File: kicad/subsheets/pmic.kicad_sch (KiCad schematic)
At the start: 53 parts, among them U2 RK809-5

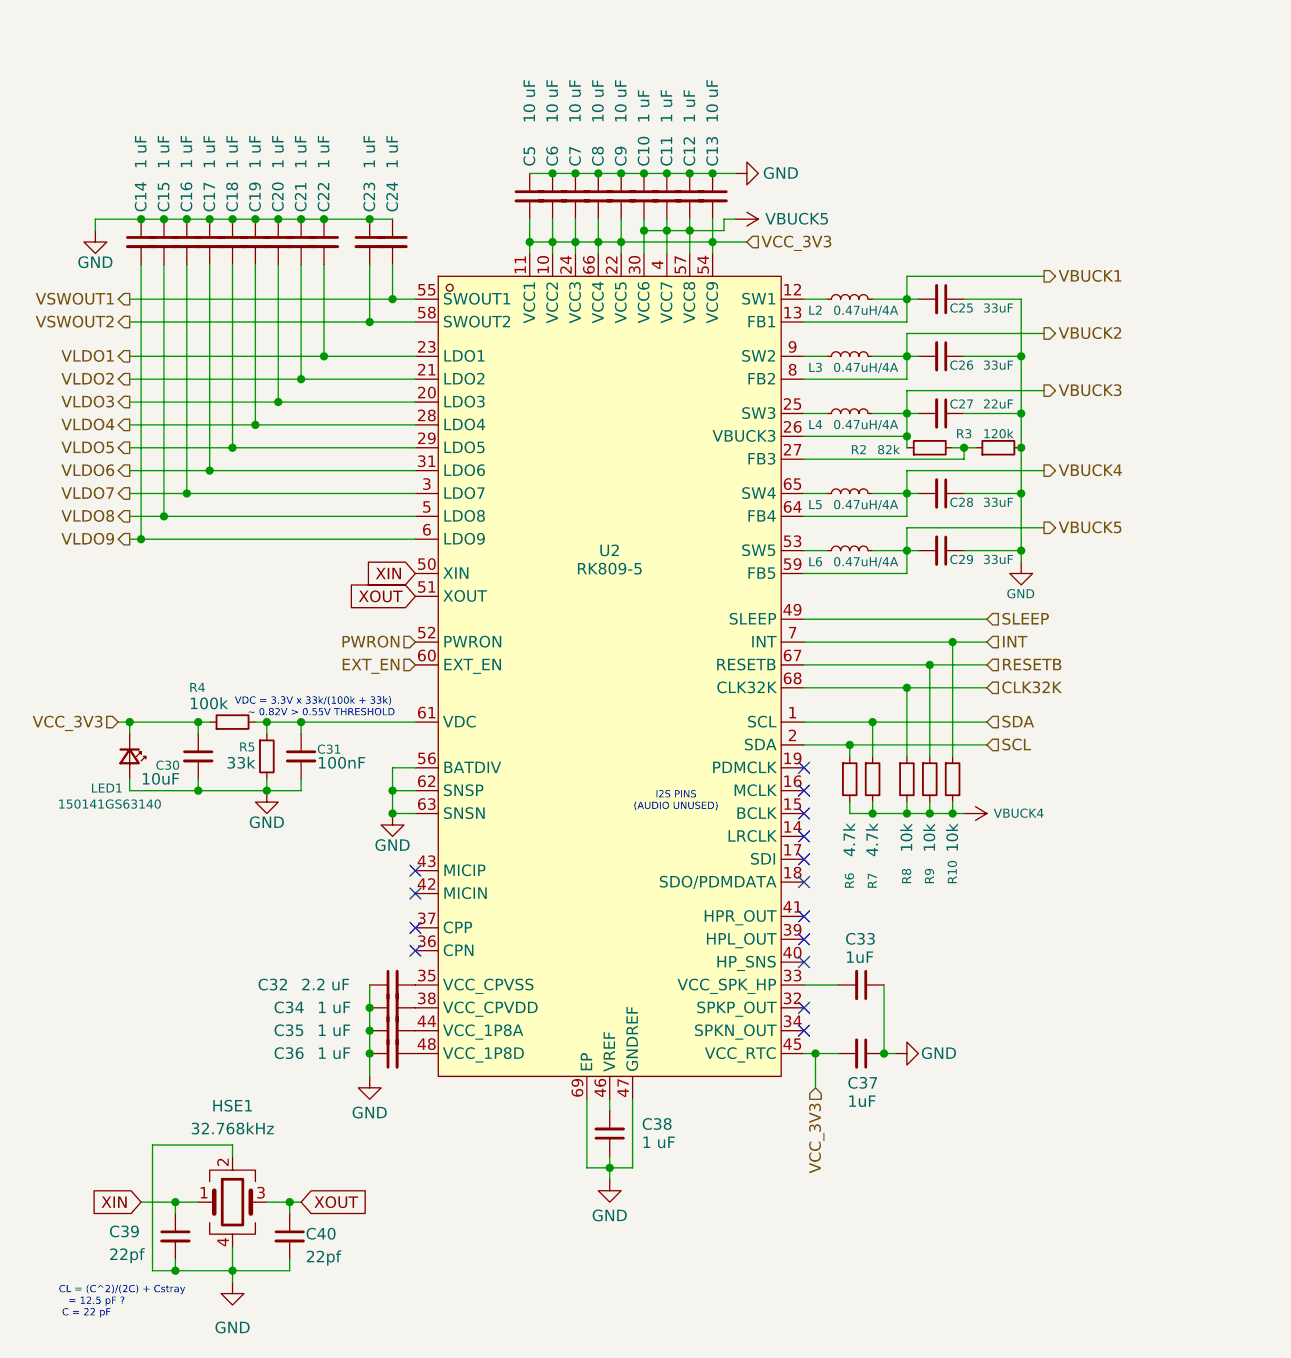
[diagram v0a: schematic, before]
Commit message: Clean up root wiring
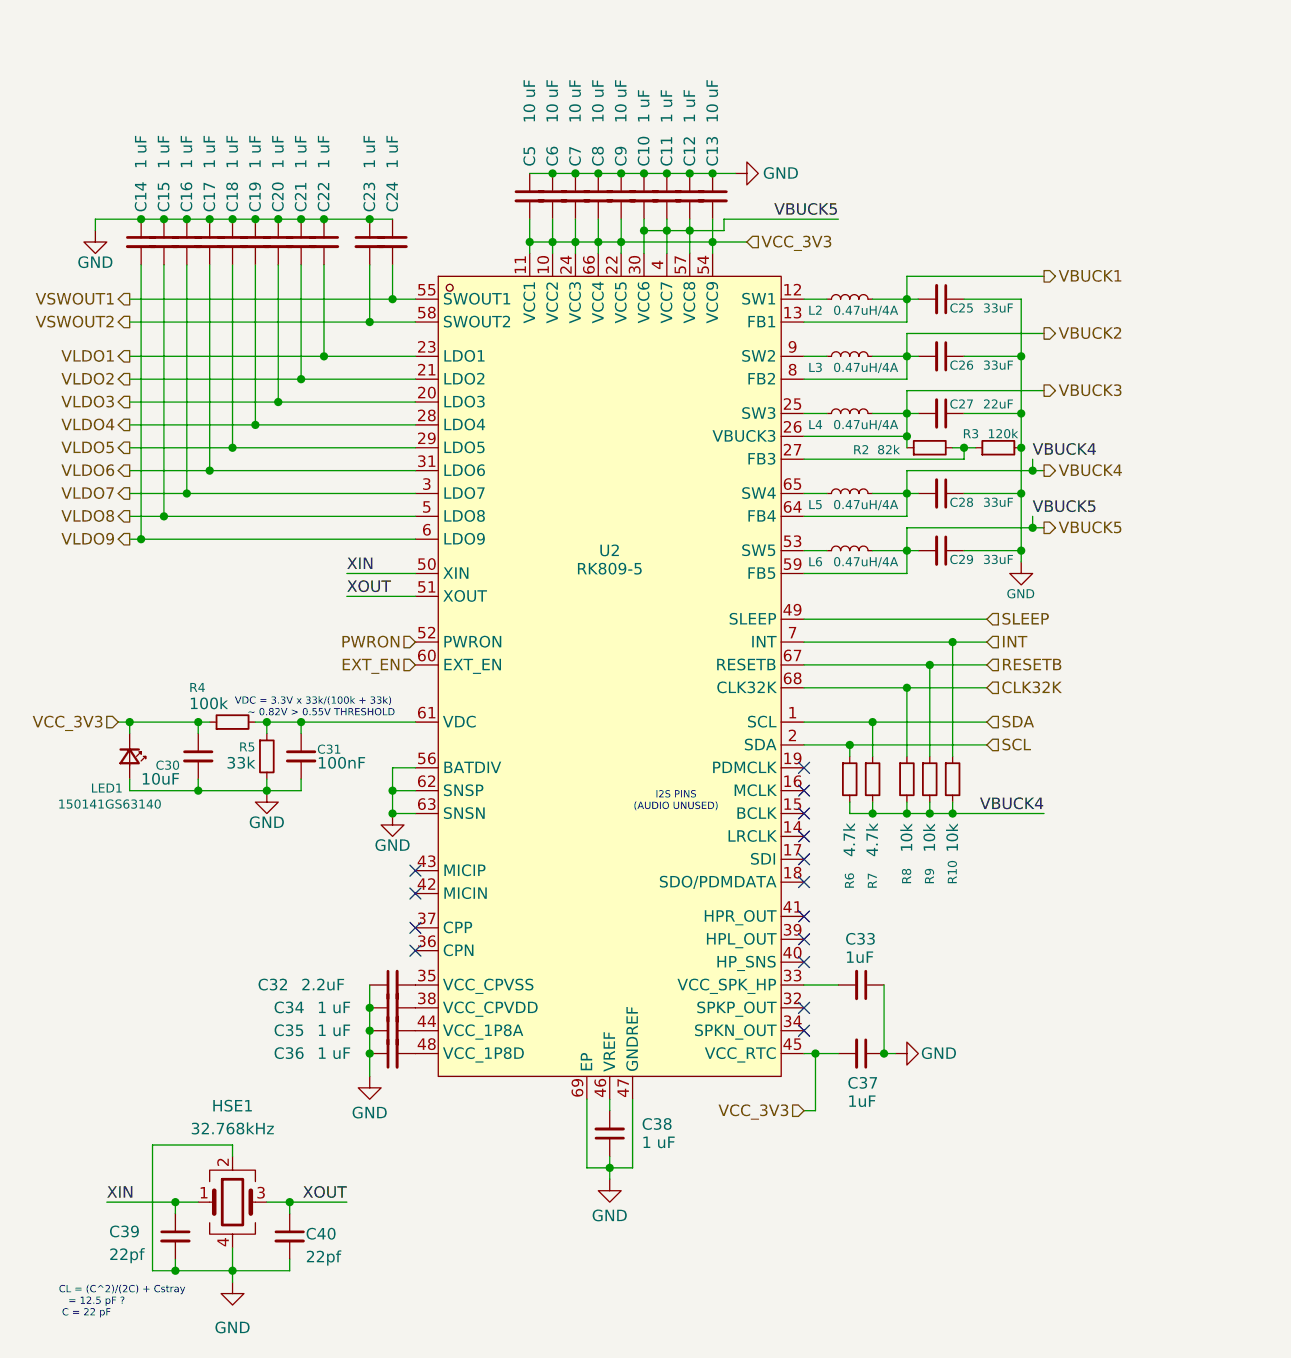
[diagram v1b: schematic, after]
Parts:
- C32: value 2.2 uF -> 2.2uF

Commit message: Wire peripherals to STM
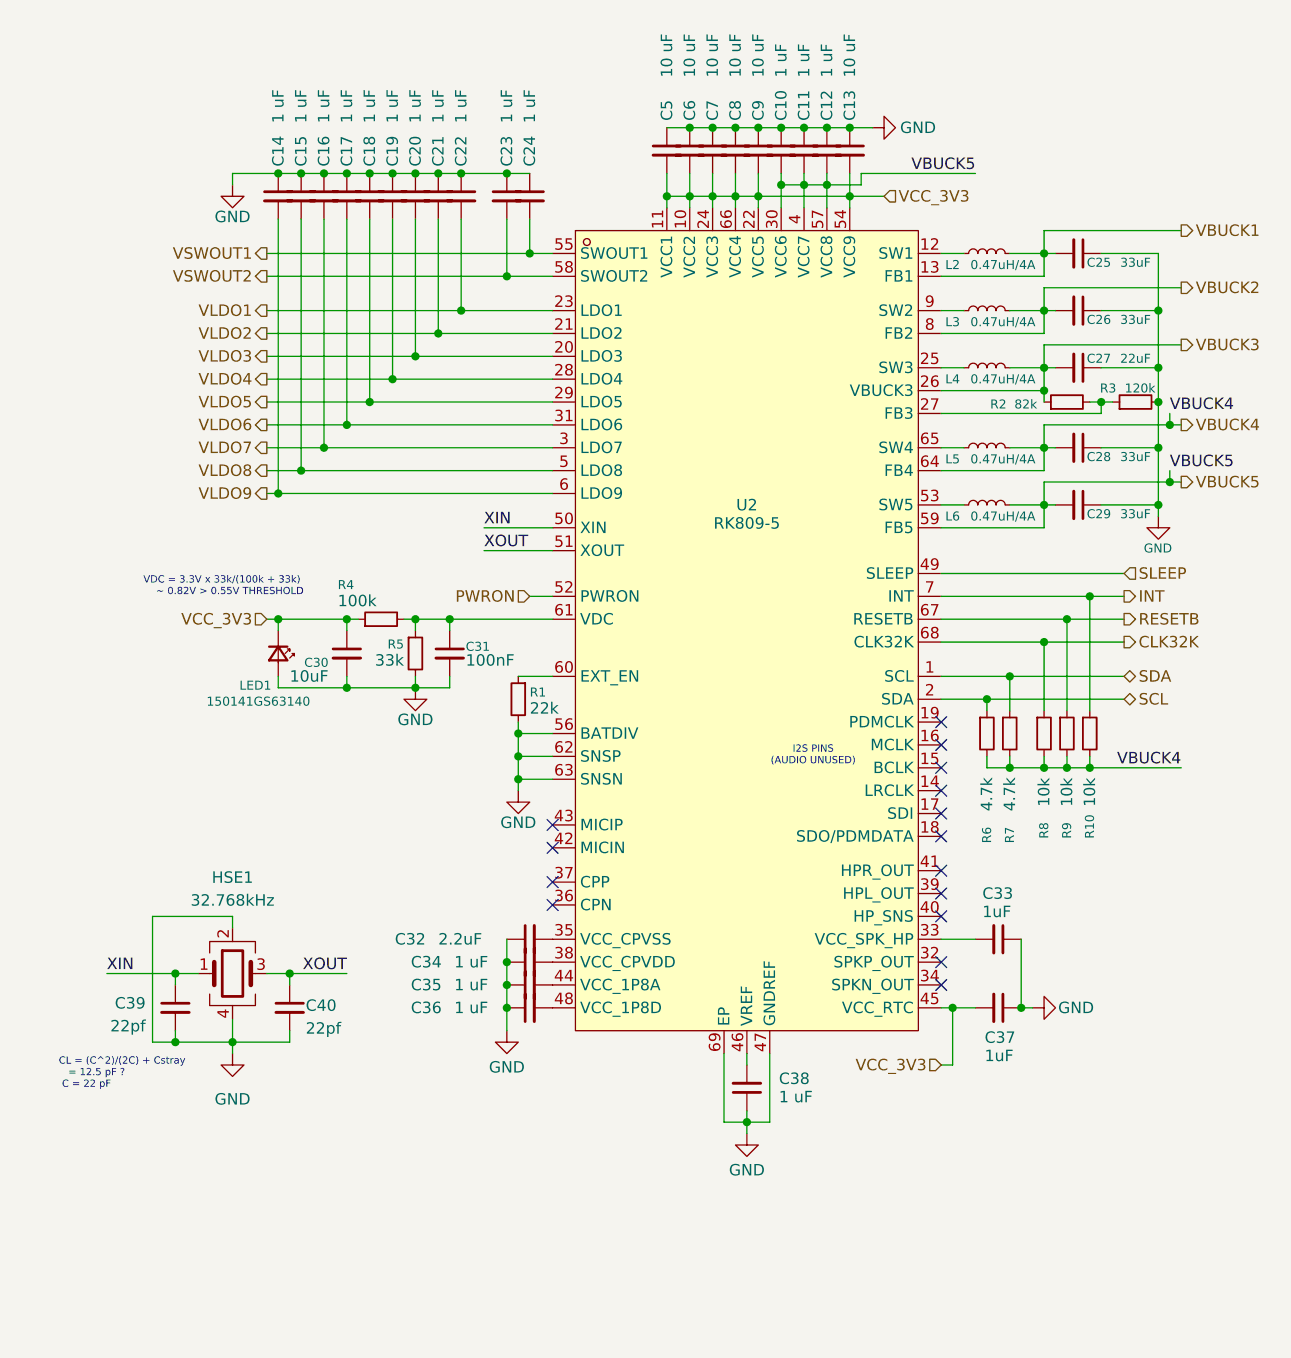
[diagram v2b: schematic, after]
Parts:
- added R1: 22k, symbol Device:R_Small
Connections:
- net GND: now also R1.2
- net EXT_EN: no longer names the net of U2.60 (EXT_EN)
- net EXT_EN: now also R1.1
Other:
- moved on the sheet: C10, C11, C12, C13, C14, C15, C16, C17, C18, C19, C20, C21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
